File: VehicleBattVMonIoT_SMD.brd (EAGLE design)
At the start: 65 x 50 mm, 55 parts, among them IC1 LD117AS33TR, J1 CON_HEADER_1X06-SMD-RIGHT-ANG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, M1 ARDUINO-PRO-MINI-3.3V#APC, U1 DC-DC-STEP-DOWN-MP1584, U2 ARDUINO_PRO_MINI, U3 RFM69HCW, X1 BU-SMA-G

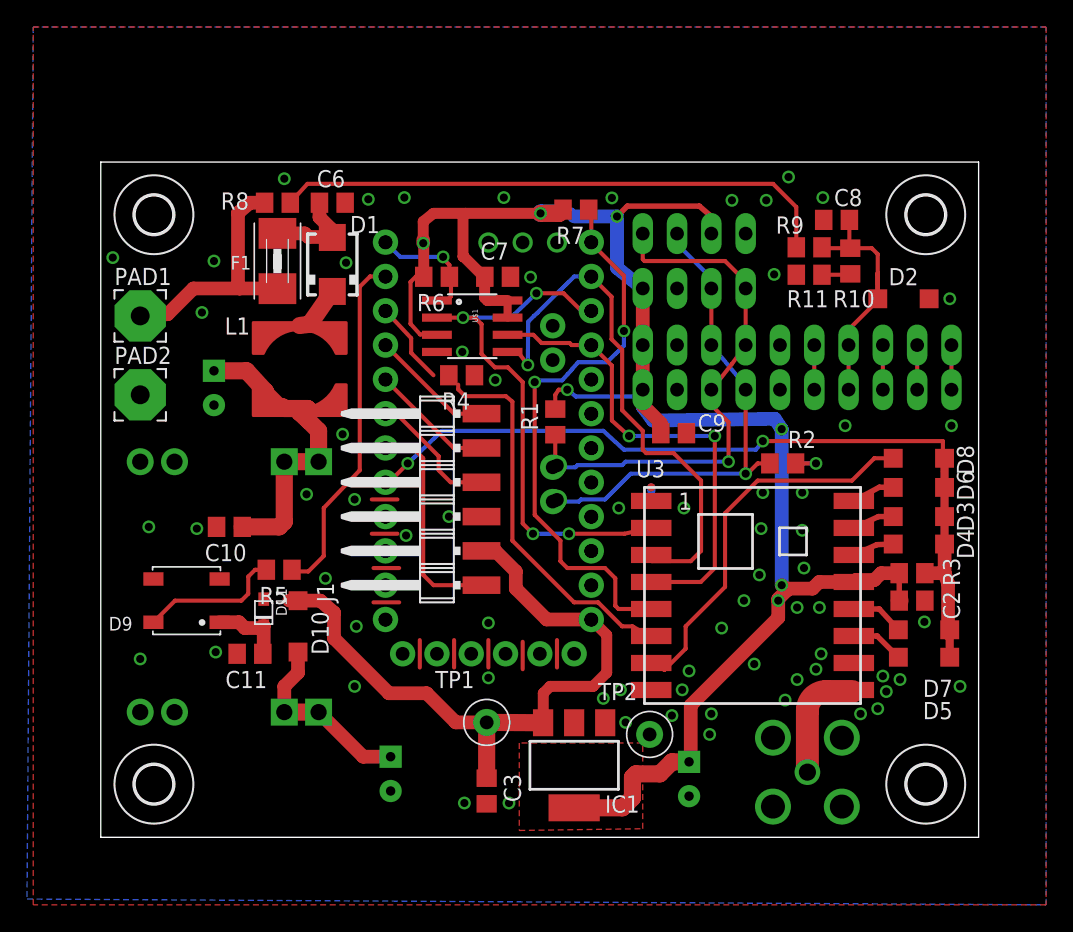
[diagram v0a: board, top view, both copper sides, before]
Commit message: updated arduino pro mini symbol to allow flood
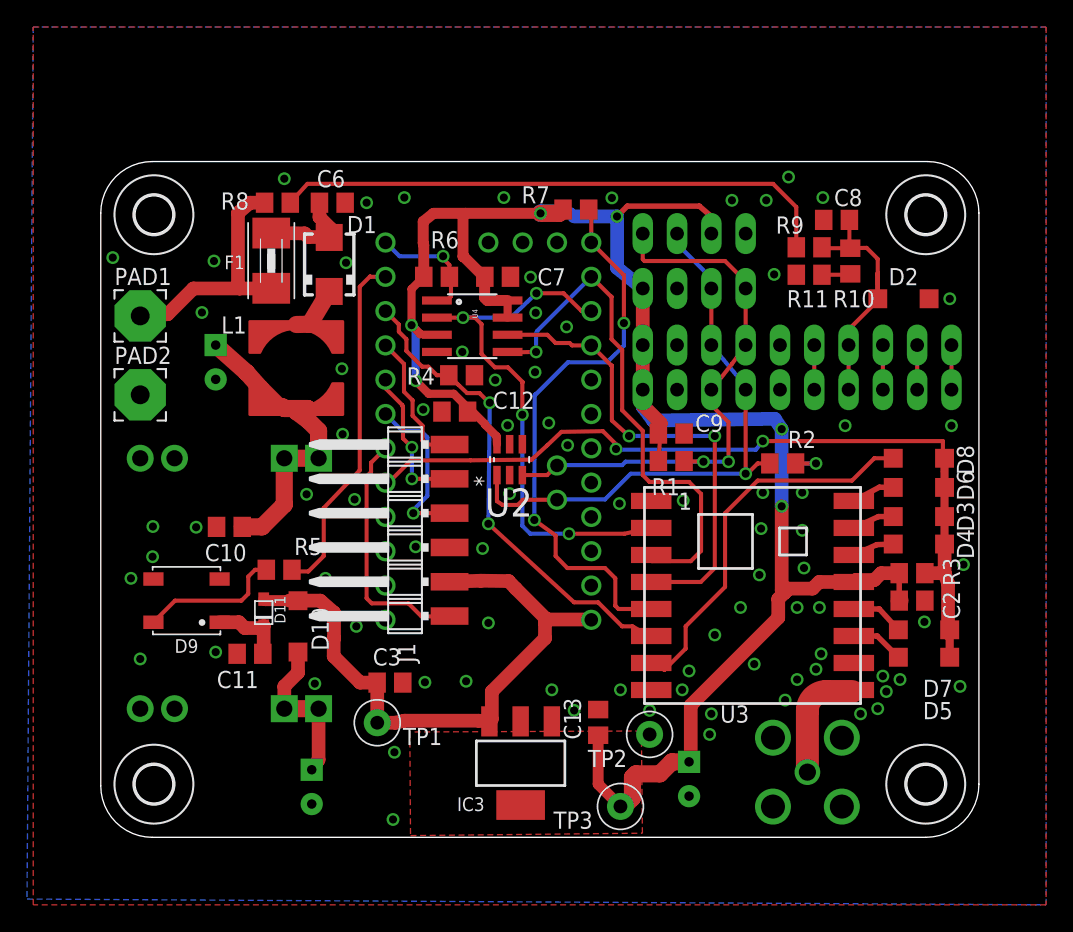
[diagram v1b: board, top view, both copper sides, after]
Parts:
- removed IC1: LD117AS33TR, v-reg:SOT223
- added C12: 100n, 0805, 25v, rcl:C0805
- added C13: 1uF, 0805, 25V, rcl:C0805
- added IC3: (no value), SparkFun-PowerIC:SOT223
- added TP3: TP_1MM_TH", TP_1MM_TH:TP_1MM_TH
- C10, C3, C9: value (none) -> 1uF, 0805, 25V
- C6: value (none) -> 100n, 0805, 25V
- U2: value ARDUINO_PRO_MINI -> 24AA025E64T-I/OT; device SparkFun-Boards:ARDUINO_PRO_MINI -> Microchip-24AA0:SOT95P280X145-6N
- moved C3 10.8 mm to (21.4, 11.5), turned to 0 degrees
- moved R1 9.06 mm to (42.2, 27.9), turned to 180 degrees
- moved TP1 8.10 mm to (20.5, 8.48)
- moved C4 5.92 mm to (15.6, 3.73)
- moved J1 3.29 mm to (22.5, 22.7)
- moved C5 1.91 mm to (8.51, 35.2)
- moved U2 1.80 mm to (30.3, 28.0), flipped to the top, turned to 90 degrees
- moved F1 0.46 mm to (12.6, 42.7)
- moved L1 0.27 mm to (14.5, 34.7)
- moved U1 0.25 mm to (9.53, 18.8)
- moved D1 0.23 mm to (16.9, 42.4)
- moved C9 0.18 mm to (42.2, 29.9)
- renumbered U$1 to U4
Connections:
- net +3V3: now also C12.1, C13.1, IC3.2, IC3.4, TP3.P$1, U2.6; no longer IC1.4
- net +5V: now also IC3.3; no longer IC1.3, U2.24
- net /INT: no longer U2.5
- net BT_BRK: no longer U2.9
- net BT_RXD: no longer U2.8
- net BT_STATE: no longer U2.6
- net BT_TXD: no longer U2.7
- net GND: now also C12.2, C13.2, IC3.1, M1.J3.1, U2.2, U2.5; no longer IC1.1, U2.23
- net MISO: no longer U2.15
- net MOSI: no longer U2.14
- net NSS_1: no longer U2.13
- net NSS_2: no longer U2.12
- net PER_RST: no longer U2.10
- net RGB_CTRL: no longer U2.11
- net SCK: no longer U2.16
- net SCL: now also U2.1; no longer U2.A5
- net SDA: now also U2.3; no longer U2.A4
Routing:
- net GND: track 18.0 -> 0.19 mm, vias 68 -> 81
- net +3V3: track 139.7 -> 150.1 mm, vias 8 -> 7
- net SCL: track 37.0 -> 43.3 mm
- net +5V: track 50.7 -> 45.2 mm
- net BT_TXD: track 9.83 -> 12.5 mm, vias 0 -> 1
- net N$5: track 14.1 -> 11.8 mm
- net BT_STATE: track 16.5 -> 18.4 mm
- net BT_RXD: track 9.22 -> 10.9 mm, vias 0 -> 2
- net SDA: track 40.6 -> 42.1 mm, vias 1 -> 2
- net MOSI: track 40.5 -> 39.2 mm
- net PER_RST: track 34.3 -> 35.6 mm, vias 0 -> 2
- net BT_BRK: track 9.21 -> 10.3 mm
- net VBATT_FUSED: track 7.15 -> 7.75 mm
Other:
- outline, holes or cut-outs redrawn

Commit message: CAD A release for manufacture
Released for manufacture at OSH park
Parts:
- removed SV2: (no value), con-lstb:MA10-1W
- removed U2: 24AA025E64T-I/OT, Microchip-24AA0:SOT95P280X145-6N
- added IC1: 24AA02E64, microchip:SOT23-5L
- added TP4, TP5, TP6, TP7, TP8: TP_1MM_TH", TP_1MM_TH:TP_1MM_TH
- C11, C2, C7: value (none) -> 1uF, 0805, 25V
- C12: value 100n, 0805, 25v -> 1u, 0805, 25v
- C6: value 100n, 0805, 25V -> 1u, 0805, 25V
- C8: value (none) -> 1n, 0805, 16v
- R4, R6, R7: value 4k7 -> 10k
- SV1: value NOFIT -> (none)
- moved R9 36.2 mm to (16.4, 47.2)
- moved C3 10.3 mm to (31.6, 13.2)
- moved D2 6.23 mm to (53.2, 39.6), turned to 180 degrees
- moved C6 4.01 mm to (17.9, 43.1), turned to 270 degrees
- moved JP2 3.69 mm to (42.3, 41.4), turned to 270 degrees
- moved H4 2.91 mm to (64.0, 46.1)
- moved H5 2.91 mm to (64.0, 3.94)
- moved C8 2.87 mm to (52.5, 43.7)
- moved JP1 2.17 mm to (46.0, 41.4), turned to 270 degrees
- moved D1 2.03 mm to (14.9, 42.4)
- moved F1 1.53 mm to (11.1, 42.6)
- moved R8 0.80 mm to (12.3, 47.2)
- moved R7 0.13 mm to (35.2, 46.6)
- moved C4 0.13 mm to (15.6, 3.86)
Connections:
- new net ARD_A0: M1.J6.8, TP4.P$1
- net +3V3: now also IC1.4; no longer SV2.1, U2.6
- net ADC_A0: now also TP8.P$1; no longer SV2.7
- net ADC_A1: now also TP5.P$1; no longer SV2.8
- net ADC_A2: now also TP6.P$1; no longer SV2.9
- net ADC_A3: now also TP7.P$1; no longer SV2.10
- net ALERT: no longer SV2.6
- net GND: now also IC1.2; no longer SV2.2, SV2.5, U2.2, U2.4, U2.5
- net SCL: now also IC1.1, R1.1, SV1.3; no longer R2.1, SV1.4, SV2.3, U2.1
- net SDA: now also IC1.3, R2.1, SV1.4; no longer R1.1, SV1.3, SV2.4, U2.3
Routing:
- net N$4: track 41.8 -> 2.16 mm
- net ADC_A0: track 21.0 -> 55.7 mm
- net SDA: track 42.1 -> 33.6 mm, vias 2 -> 1
- net ARD_A0: track 0.00 -> 3.38 mm
- net ALERT: track 3.30 -> 0.00 mm
- net +3V3: track 150.1 -> 148.1 mm
- net VBATT: track 19.3 -> 17.9 mm
- net N$2: track 3.81 -> 2.52 mm
- net SCL: track 43.3 -> 42.1 mm, vias 1 -> 2
- net +5V: track 45.2 -> 44.6 mm
- net ADC_A3: track 3.30 -> 3.81 mm
- net ADC_A2: track 3.30 -> 3.81 mm
- net ADC_A1: track 3.30 -> 3.81 mm
- net GND: vias 81 -> 105
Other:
- board size 65 x 50 mm -> 68 x 50 mm
